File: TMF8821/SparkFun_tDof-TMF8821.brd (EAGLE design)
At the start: 25.4 x 25.4 mm, 56 parts, among them J4 QWIIC_RIGHT_ANGLE, J5 QWIIC_RIGHT_ANGLE

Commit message: Adds "TMF8821" silk to the 8821 board design files
* Replaces device with TMF8821 in schematic and updates text
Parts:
- U$1: value TMF8820- -> TMF8821-
- U$11: device TMFTopSilk:TMF88209 -> TMFTopSilk:TMF8821882022
- U$26: device TMFTopSilk:TMF882021 -> TMFTopSilk:TMF8821882022
- moved U$11 0.18 mm to (51.3, 39.6)
- moved U$26 0.13 mm to (45.6, 38.0)
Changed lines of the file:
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@@
 </element>
 <element name="U$25" library="SparkFun-Aesthetics" package="SFE_LOGO_FLAME_.1" value="" x="56.642" y="34.29" smashed="yes" rot="R90"/>
-<element name="U$1" library="TMF882X" package="TMF882X" value="TMF8820-" x="45.72" y="39.37" smashed="yes">
+<element name="U$1" library="TMF882X" package="TMF882X" value="TMF8821-" x="45.72" y="39.37" smashed="yes">
 <attribute name="NAME" x="43.9928" y="41.9354" size="0.6096" layer="25" font="vector" ratio="20"/>
-<attribute name="PROD_ID" value="IC-16432" x="45.72" y="39.37" size="1.778" layer="27" font="vector" ratio="15" display="off"/>
+<attribute name="PROD_ID" value="IC-16433" x="45.72" y="39.37" size="1.778" layer="27" font="vector" ratio="15" display="off"/>
 <attribute name="VALUE" x="43.7388" y="36.1188" size="0.6096" layer="27" font="vector" ratio="20"/>
 </element>
@@
 <element name="U$7" library="TMFTopSilk" package="#EN#7" value="" x="41.91" y="48.641" smashed="yes" rot="R90"/>
 <element name="U$10" library="TMFTopSilk" package="##INT##8" value="" x="49.53" y="48.387" smashed="yes" rot="R90"/>
-<element name="U$11" library="TMFTopSilk" package="TMF88209" value="" x="51.181" y="39.497" smashed="yes" rot="R90"/>
 <element name="U$12" library="TMFTopSilk" package="DTOF882188211" value="" x="49.784" y="39.37" smashed="yes" rot="R90"/>
 <element name="U$13" library="SparkFun-Aesthetics" package="SFE_LOGO_NAME_.1" value="" x="41.021" y="39.116" smashed="yes" rot="R90"/>
@@
 <element name="U$23" library="TMFBotSilk" package="#SDA#6" value="" x="46.99" y="30.607" smashed="yes" rot="MR270"/>
 <element name="U$24" library="TMFBotSilk" package="#SYNC#8" value="" x="46.99" y="47.625" smashed="yes" rot="MR270"/>
-<element name="U$26" library="TMFTopSilk" package="TMF882021" value="" x="45.466" y="37.973" smashed="yes" rot="MR0"/>
 <element name="U$27" library="TMFTopSilk" package="DTOF8821882023" value="" x="45.466" y="39.243" smashed="yes" rot="MR0"/>
 <element name="U$28" library="TMFBotSilk" package="DEF11" value="" x="54.737" y="34.925" smashed="yes" rot="MR0"/>
 <element name="U$29" library="TMFBotSilk" package="ADDR#12" value="" x="50.927" y="34.925" smashed="yes" rot="MR0"/>
 <element name="U$30" library="TMFBotSilk" package="0X4113" value="" x="52.959" y="33.528" smashed="yes" rot="MR0"/>
+<element name="U$11" library="TMFTopSilk" package="TMF8821882022" value="" x="51.308" y="39.624" smashed="yes" rot="R90"/>
+<element name="U$26" library="TMFTopSilk" package="TMF8821882022" value="" x="45.593" y="37.973" smashed="yes" rot="MR0"/>
 </elements>
 <signals>

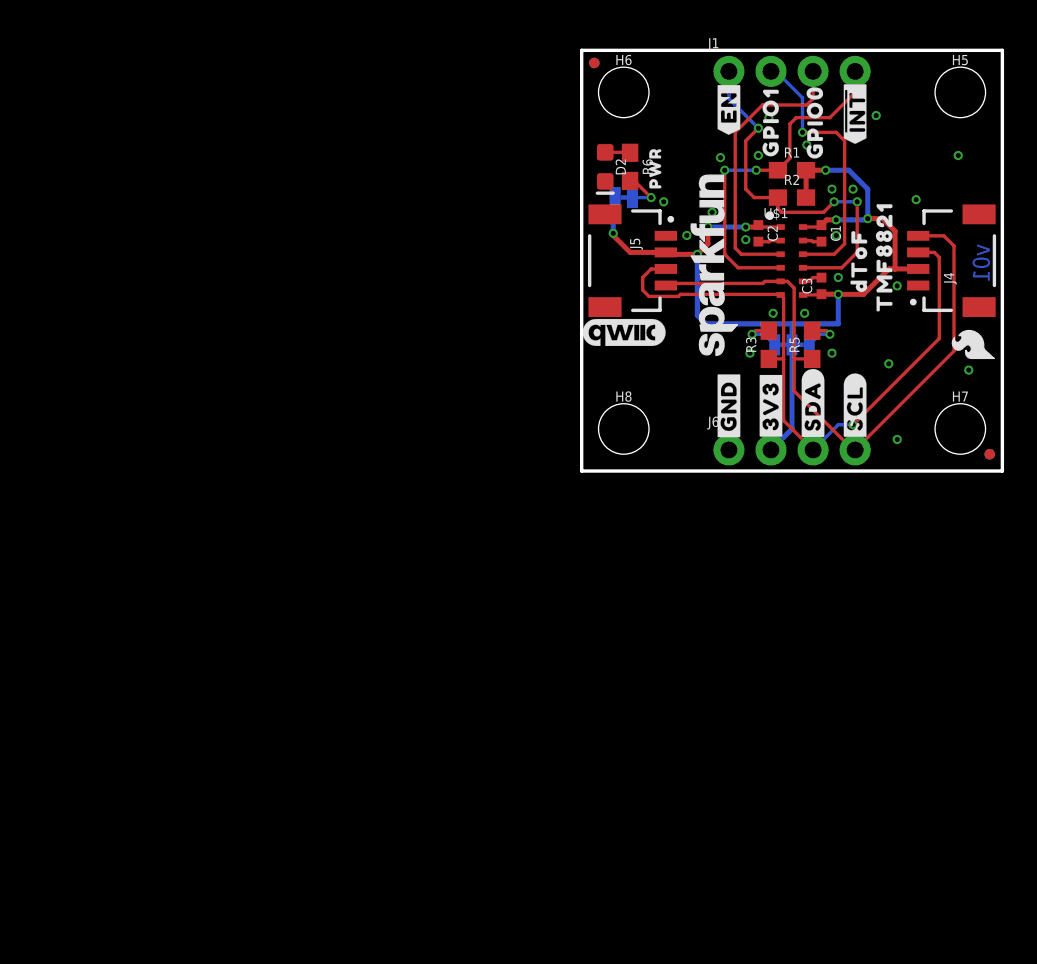
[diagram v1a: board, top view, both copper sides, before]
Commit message: Copies 8820 designs to create 8821 designs - updates relevant references to 8820 to 8821
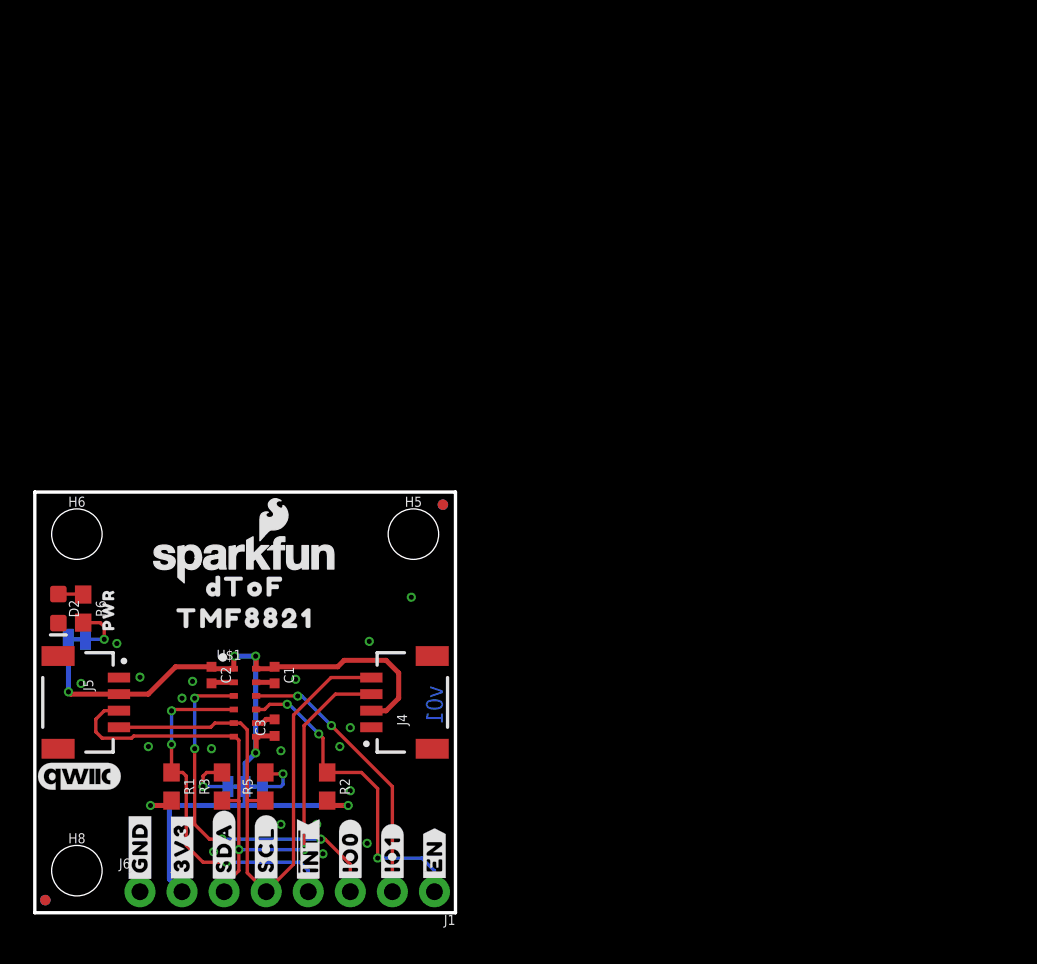
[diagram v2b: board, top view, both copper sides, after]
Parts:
- removed H7: STAND-OFFTIGHT, SparkFun-Hardware:STAND-OFF-TIGHT
- removed U$27: (no value), TMFTopSilk:DTOF8821882023
- U$1: value TMF8821- -> TMF882X_TMF8821
- U$10: device TMFTopSilk:##INT##8 -> TMFBotSilk:##INT##9
- U$11, U$26: device TMFTopSilk:TMF8821882022 -> TMFTopSilk:DTOF882188211
- U$12: device TMFTopSilk:DTOF882188211 -> TMFTopSilk:TMF882188210
- U$13: device SparkFun-Aesthetics:SFE_LOGO_NAME_.1 -> SparkFun-Aesthetics:SFE_LOGO_NAME_FLAME_.1
- U$15: device TMFBotSilk:##INT##9 -> TMFBotSilk:#SYNC#8
- U$19: device TMFBotSilk:#GPIO1#8 -> TMFTopSilk:#IO0#8
- U$24: device TMFBotSilk:#SYNC#8 -> TMFTopSilk:##INT##8
- U$25: device SparkFun-Aesthetics:SFE_LOGO_FLAME_.1 -> TMFTopSilk:TMF882188210
- U$8: device TMFTopSilk:GPIO18 -> TMFTopSilk:#IO0#8
- U$9: device TMFTopSilk:GPIO019 -> TMFTopSilk:#IO1#8
- moved FD5 63.1 mm to (0.64, 0.76)
- moved FD8 63.1 mm to (0.64, 0.76)
- moved U$10 55.6 mm to (16.5, 3.68)
- moved U$24 53.5 mm to (16.5, 3.68)
- moved R1 52.8 mm to (8.26, 7.62), turned to 270 degrees
- moved J1 52.6 mm to (24.1, 1.27), turned to 180 degrees
- moved U$15 52.1 mm to (21.6, 4.45)
- moved U$9 51.0 mm to (21.6, 3.56)
- moved U$8 50.9 mm to (19.1, 3.68)
- moved U$19 50.6 mm to (19.1, 3.68), turned to 90 degrees
- moved U$30 49.6 mm to (8.51, 11.6)
- moved U$17 48.6 mm to (24.1, 3.43), flipped to the top, turned to 90 degrees
- moved U$7 48.6 mm to (24.1, 3.43), flipped to the bottom, turned to 270 degrees
- moved U$25 46.9 mm to (12.7, 17.8), flipped to the bottom, turned to 0 degrees
- moved R2 45.3 mm to (17.7, 7.62), turned to 270 degrees
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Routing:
- net GPIO0/SYNC: track 17.1 -> 22.1 mm, vias 0 -> 4
- net EN: track 22.8 -> 19.8 mm
- net SCL: track 38.2 -> 36.4 mm
- net !INT!: track 21.1 -> 22.0 mm, vias 2 -> 3
- net 3.3V: track 60.3 -> 61.1 mm, vias 8 -> 6
- net N$7: track 2.74 -> 3.37 mm
- net SDA: track 38.7 -> 38.1 mm, vias 1 -> 2
- net GPIO1: track 16.4 -> 16.8 mm, vias 1 -> 2
- net GND: track 3.73 -> 3.72 mm, vias 23 -> 20
